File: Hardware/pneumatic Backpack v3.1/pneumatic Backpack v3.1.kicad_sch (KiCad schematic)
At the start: 32 parts, among them J1 Conn_01x12_Pin, J10 Conn_01x02_Pin, J11 Conn_01x02_Pin, J2 Conn_01x01_Pin, J5 Conn_01x12_Pin, J9 Conn_01x02_Pin, U1 ESP32-S3-DEVKITC-1-N8R2, U5 MCZ33996EK

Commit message: updated
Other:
- moved on the sheet: D10, D11, D12, D13, D14, D15, D16, D9, J1

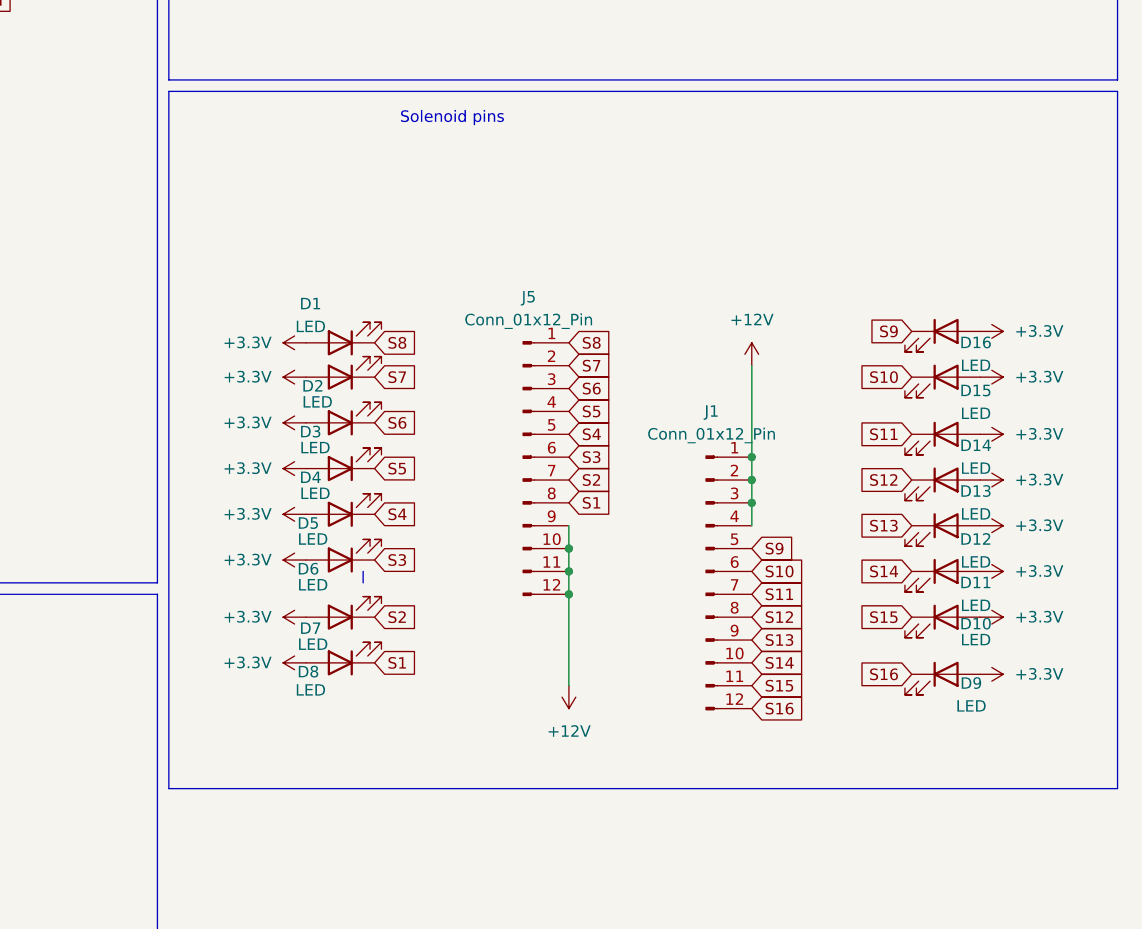
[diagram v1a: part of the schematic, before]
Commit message: added diods to the leds
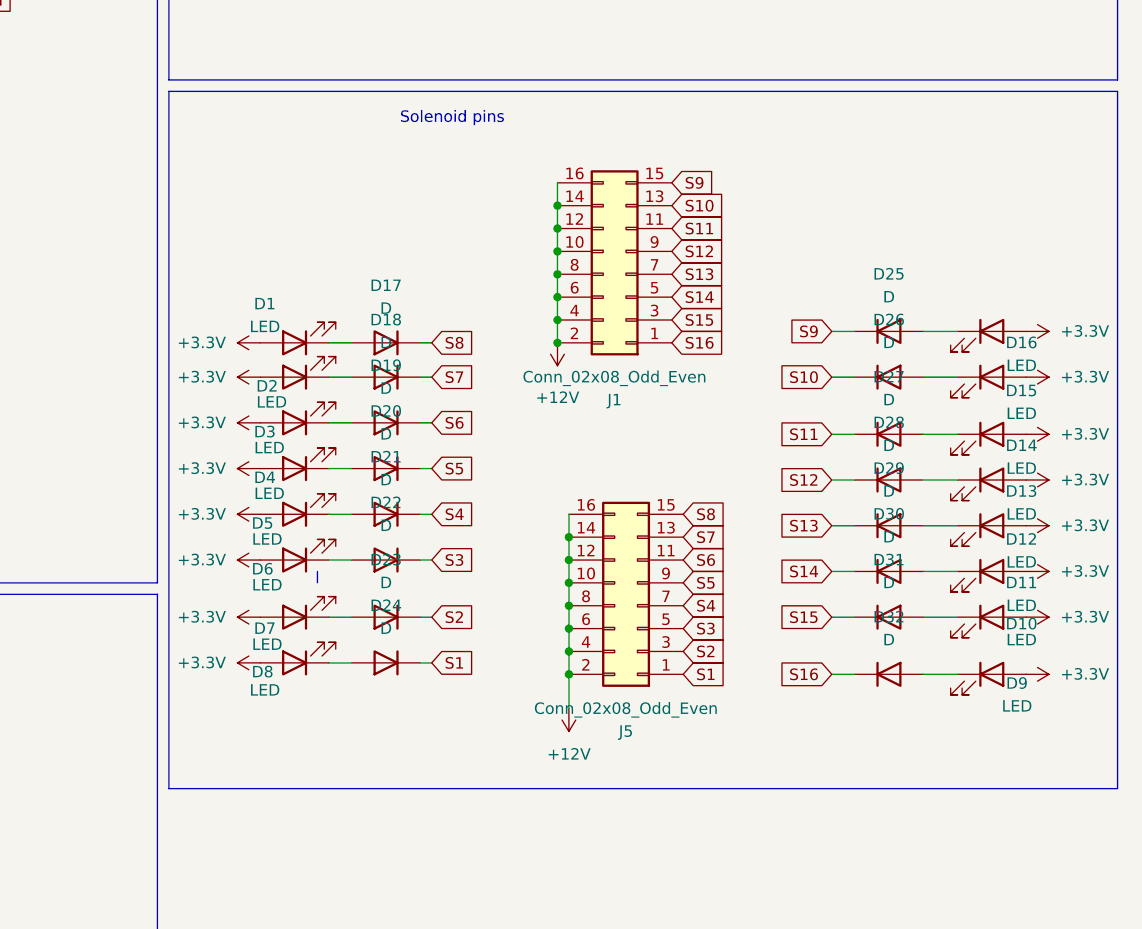
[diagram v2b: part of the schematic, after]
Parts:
- removed J1, J5: Conn_01x12_Pin, Connector_JST:JST_ZH_B12B-ZR_1x12_P1.50mm_Vertical, symbol Connector:Conn_01x12_Pin
- added D17, D18, D19, D20, D21, D22, D23, D24, D25, D26, D27, D28, D29, D30, D31, D32: D, Diode_SMD:D_0805_2012Metric_Pad1.15x1.40mm_HandSolder, symbol Device:D
- added J1, J5: Conn_02x08_Odd_Even, Connector_JST:JST_PHD_S16B-PHDSS_2x08_P2.00mm_Horizontal, symbol Connector_Generic:Conn_02x08_Odd_Even
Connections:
- net +12V: now also J1.10 (Pin_10), J1.12 (Pin_12), J1.14 (Pin_14), J1.16 (Pin_16), J1.2 (Pin_2), J1.4 (Pin_4), J1.6 (Pin_6), J1.8 (Pin_8), J5.10 (Pin_10), J5.12 (Pin_12), J5.14 (Pin_14), J5.16 (Pin_16), J5.2 (Pin_2), J5.4 (Pin_4), J5.6 (Pin_6), J5.8 (Pin_8)
- net S1: now also D24.1 (K), J5.1 (Pin_1); no longer D8.1 (K)
- net S10: now also D26.1 (K), J1.13 (Pin_13); no longer D15.1 (K)
- net S11: now also D27.1 (K), J1.11 (Pin_11); no longer D14.1 (K)
- net S12: now also D28.1 (K), J1.9 (Pin_9); no longer D13.1 (K)
- net S13: now also D29.1 (K), J1.7 (Pin_7); no longer D12.1 (K)
- net S14: now also D30.1 (K), J1.5 (Pin_5); no longer D11.1 (K)
- net S15: now also D31.1 (K), J1.3 (Pin_3); no longer D10.1 (K)
- net S16: now also D32.1 (K), J1.1 (Pin_1); no longer D9.1 (K)
- net S2: now also D23.1 (K), J5.3 (Pin_3); no longer D7.1 (K)
- net S3: now also D22.1 (K), J5.5 (Pin_5); no longer D6.1 (K)
- net S4: now also D21.1 (K), J5.7 (Pin_7); no longer D5.1 (K)
- net S5: now also D20.1 (K), J5.9 (Pin_9); no longer D4.1 (K)
- net S6: now also D19.1 (K), J5.11 (Pin_11); no longer D3.1 (K)
- net S7: now also D18.1 (K), J5.13 (Pin_13); no longer D2.1 (K)
- net S8: now also D17.1 (K), J5.15 (Pin_15); no longer D1.1 (K)
- net S9: now also D25.1 (K), J1.15 (Pin_15); no longer D16.1 (K)
- new net: D22.2 (A), D6.1 (K)
- new net: D18.2 (A), D2.1 (K)
- new net: D24.2 (A), D8.1 (K)
- new net: D15.1 (K), D26.2 (A)
- new net: D20.2 (A), D4.1 (K)
- new net: D14.1 (K), D27.2 (A)
- new net: D23.2 (A), D7.1 (K)
- new net: D11.1 (K), D30.2 (A)
- new net: D1.1 (K), D17.2 (A)
- new net: D10.1 (K), D31.2 (A)
- new net: D19.2 (A), D3.1 (K)
- new net: D12.1 (K), D29.2 (A)
- new net: D32.2 (A), D9.1 (K)
- new net: D21.2 (A), D5.1 (K)
- new net: D16.1 (K), D25.2 (A)
- new net: D13.1 (K), D28.2 (A)
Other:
- moved on the sheet: D1, D10, D11, D12, D13, D14, D15, D16, D2, D3, D4, D5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
